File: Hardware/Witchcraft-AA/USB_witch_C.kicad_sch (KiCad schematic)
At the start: 11 parts, among them J0 USB_C_Molex_201267-0005, J1 USB_C_Molex_201267-0005, U1 Z1 extreme

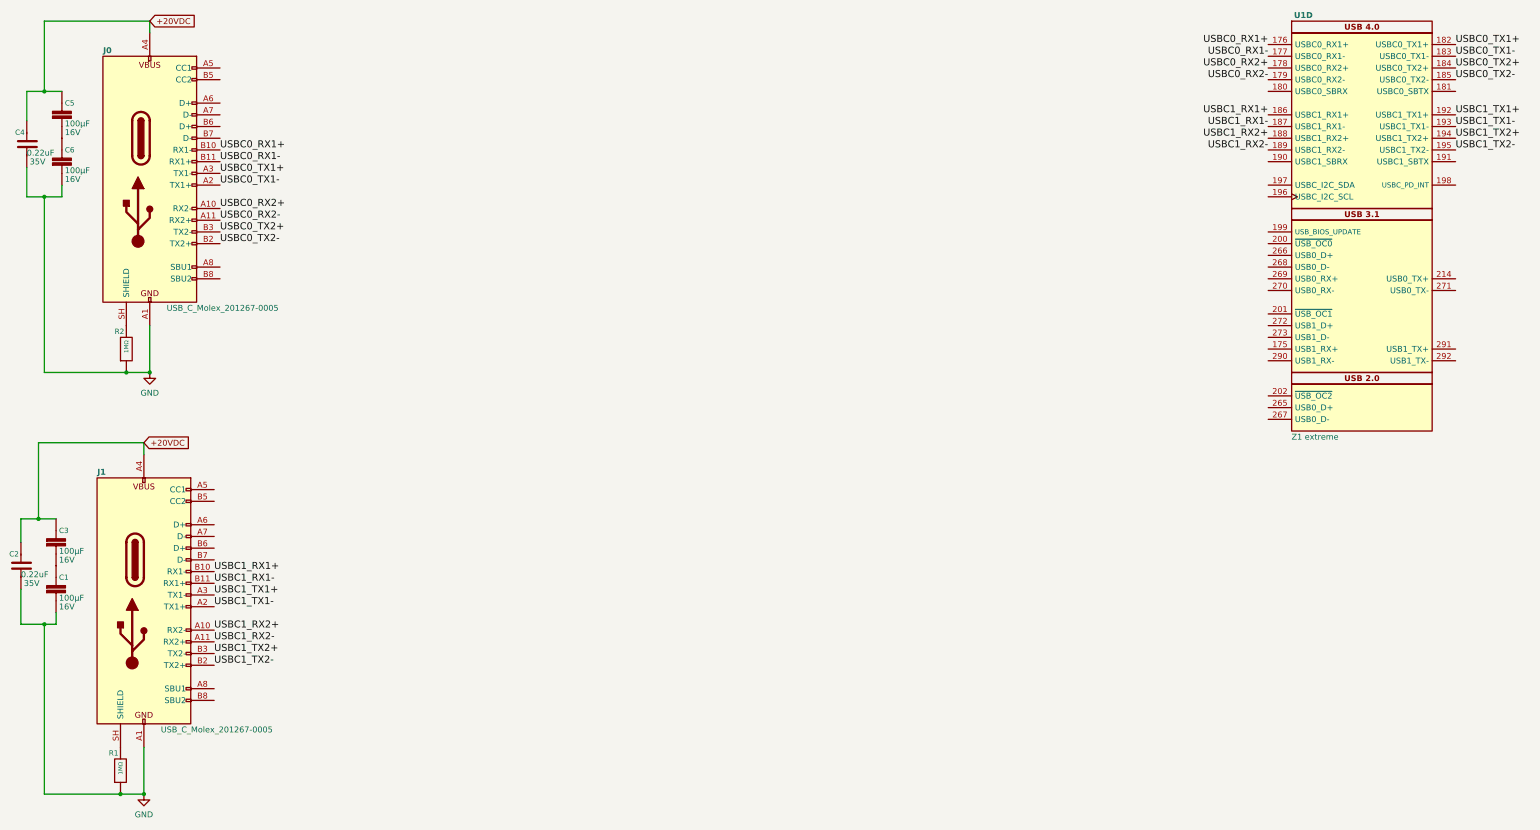
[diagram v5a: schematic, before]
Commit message: Almost completed the design of the new finstack, and have begun work on a redesign of cold-plate and rearrangement of components
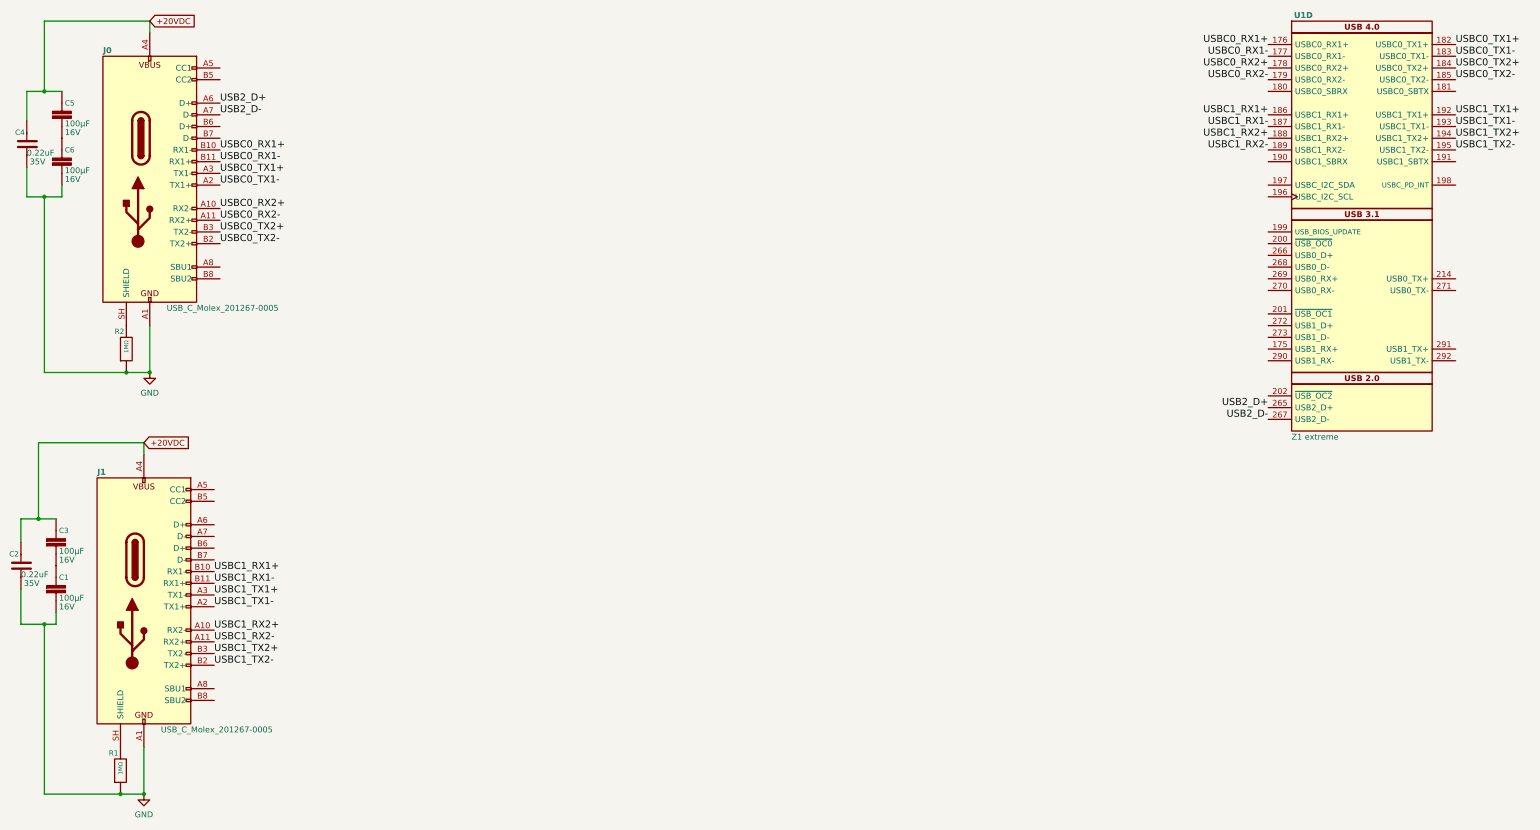
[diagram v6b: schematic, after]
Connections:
- net USB2_D+: now reaches J0.A6 (D+)
- net USB2_D+: now also U1.265 (USB2_D+)
- net USB2_D-: now reaches J0.A7 (D-)
- net USB2_D-: now also U1.267 (USB2_D-)
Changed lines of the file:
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@@
+    (effects (font (size 1.524 1.524)) (justify left bottom))
+  )
+  (label "USB2_D+" (at 73.66 45.72 0) (fields_autoplaced)
     (effects (font (size 1.524 1.524)) (justify left bottom))
   )
@@
     (effects (font (size 1.524 1.524)) (justify left bottom))
   )
+  (label "USB2_D+" (at 300.99 111.76 180) (fields_autoplaced)
+    (effects (font (size 1.524 1.524)) (justify right bottom))
+  )
   (label "USBC1_TX2+" (at 72.39 165.1 0) (fields_autoplaced)
     (effects (font (size 1.524 1.524)) (justify left bottom))
+  )
+  (label "USB2_D-" (at 300.99 114.3 180) (fields_autoplaced)
+    (effects (font (size 1.524 1.524)) (justify right bottom))
   )
   (label "USBC0_TX2-" (at 341.63 40.64 0) (fields_autoplaced)
@@
     (effects (font (size 1.524 1.524)) (justify right bottom))
   )
+  (label "USB2_D-" (at 73.66 48.26 0) (fields_autoplaced)
+    (effects (font (size 1.524 1.524)) (justify left bottom))
+  )
   (label "USBC0_RX2-" (at 300.99 40.64 180) (fields_autoplaced)
